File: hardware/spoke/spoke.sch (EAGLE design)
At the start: 3 parts, among them J1 ICSP, U1 ATMEGA328P_PDIP

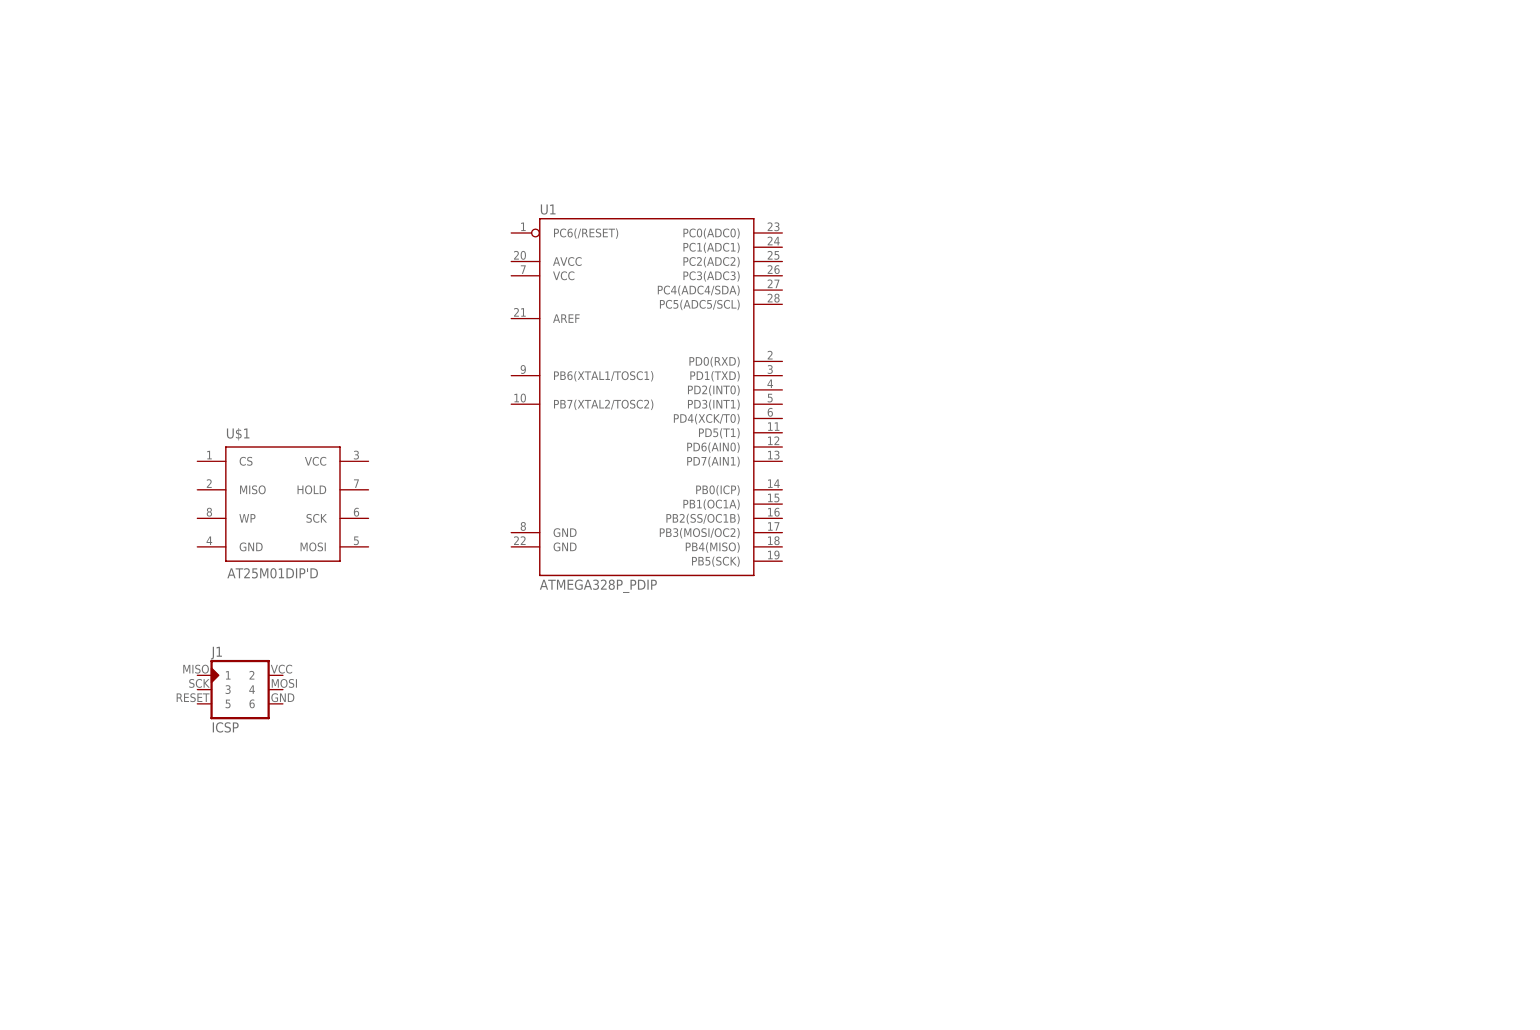
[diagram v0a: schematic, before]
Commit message: Update spoke schematic
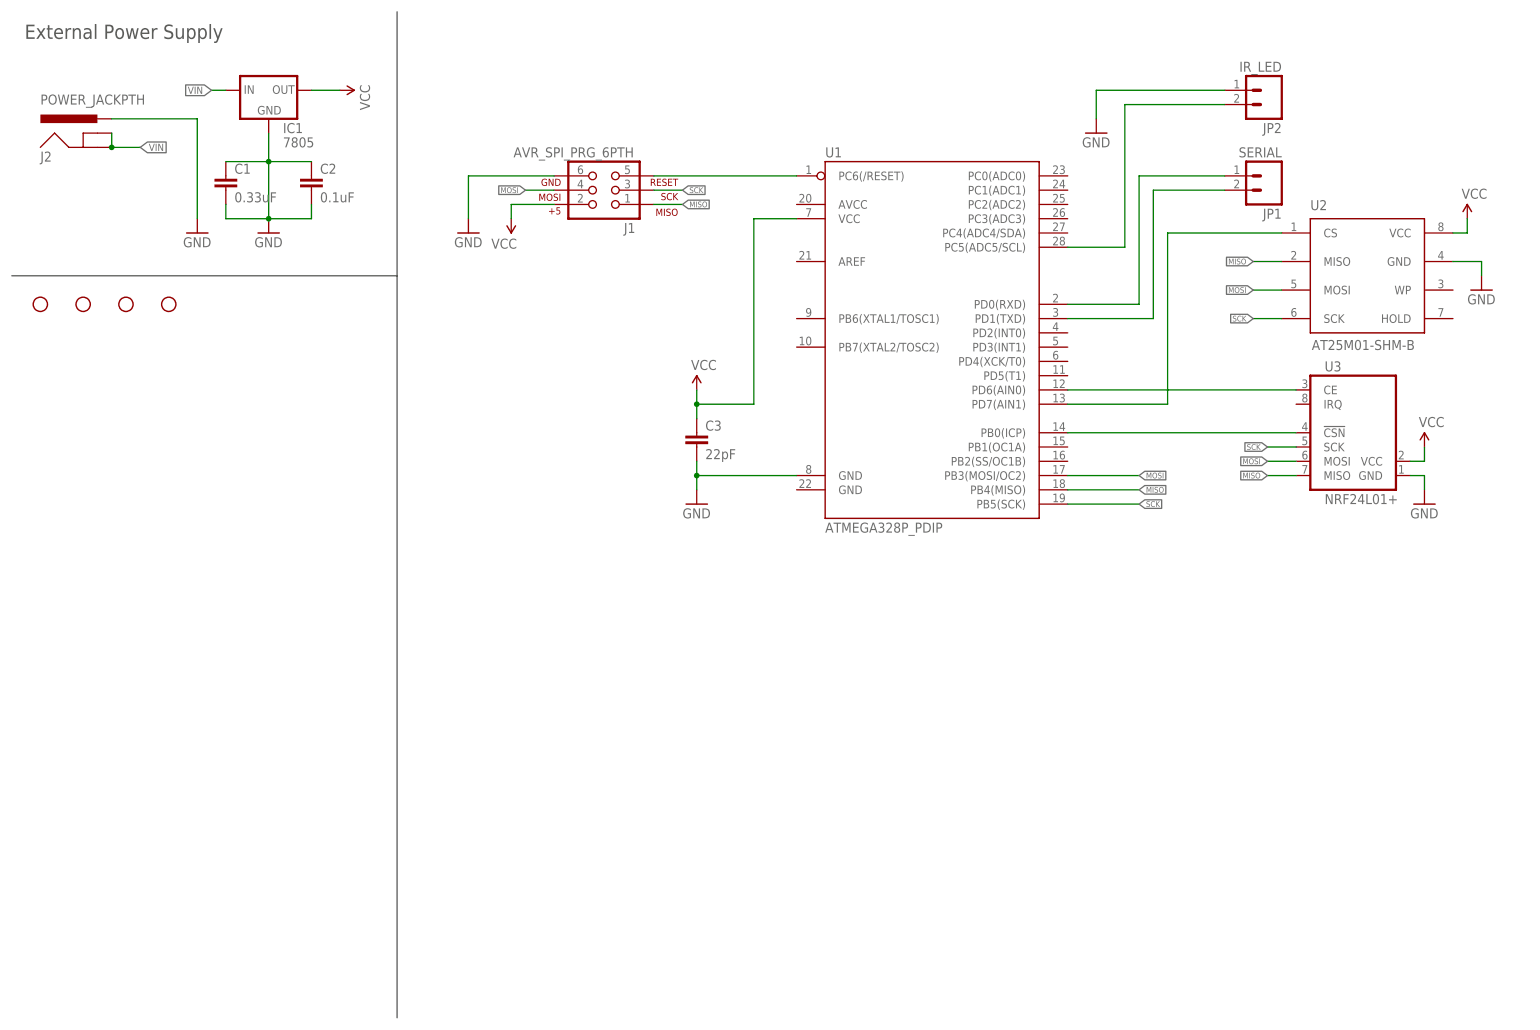
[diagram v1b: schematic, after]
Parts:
- removed U$1: AT25M01DIP'D, aurai:AT25M01DIP'D
- added C1: 0.33uF, SparkFun-Capacitors:CAPPTH
- added C2: 0.1uF, SparkFun-Capacitors:CAPPTH
- added C3: 22pF, SparkFun-Capacitors:CAPEZ
- added IC1: 7805, SparkFun-PowerIC:V_REG_78XXSINK
- added J2: POWER_JACKPTH, SparkFun-Connectors:POWER_JACKPTH
- added JP1: SERIAL, SparkFun-Connectors:M02PTH
- added JP2: IR_LED, SparkFun-Connectors:M02PTH
- added STANDOFF1, STANDOFF2, STANDOFF3, STANDOFF4: STAND-OFF, SparkFun-Electromechanical:STAND-OFF
- added U2: AT25M01-SHM-B, aurai:AT25M01-SHM-B
- added U3: NRF24L01+, aurai:NRF24L01+
- J1: value ICSP -> AVR_SPI_PRG_6PTH; device avr-isp:AVR-ISP-6PINAVR-ISP-6PIN-SMALL-SILK -> SparkFun-Connectors:AVR_SPI_PRG_6PTH
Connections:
- new net GND: C1.1, C1.2, C2.1, C2.2, C3.2, IC1.GND, J1.6, J2.PWR, JP2.1, U1.GND@1, U2.GND, U3.GND
- new net MISO: J1.1, U1.PB4(MISO), U2.MISO, U3.MISO
- new net MOSI: J1.4, U1.PB3(MOSI/OC2), U2.MOSI, U3.MOSI
- new net N$1: J1.5, U1.PC6(/RESET)
- new net N$2: JP1.1, U1.PD0(RXD)
- new net N$3: U1.PD7(AIN1), U2.CS
- new net N$4: JP1.2, U1.PD1(TXD)
- new net N$5: U1.PD6(AIN0), U3.CE
- new net N$6: JP2.2, U1.PC5(ADC5/SCL)
- new net N$7: U1.PB0(ICP), U3.!CSN
- new net SCK: J1.3, U1.PB5(SCK), U2.SCK, U3.SCK
- new net VCC: C3.1, IC1.OUT, J1.2, U1.VCC, U2.VCC, U3.VCC
- new net VIN: IC1.IN, J2.GND, J2.GNDBREAK
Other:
- note added: "External Power Supply"
- moved on the sheet: U1

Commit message: Schematic update for spoke. Added DHT-11 and LEDS
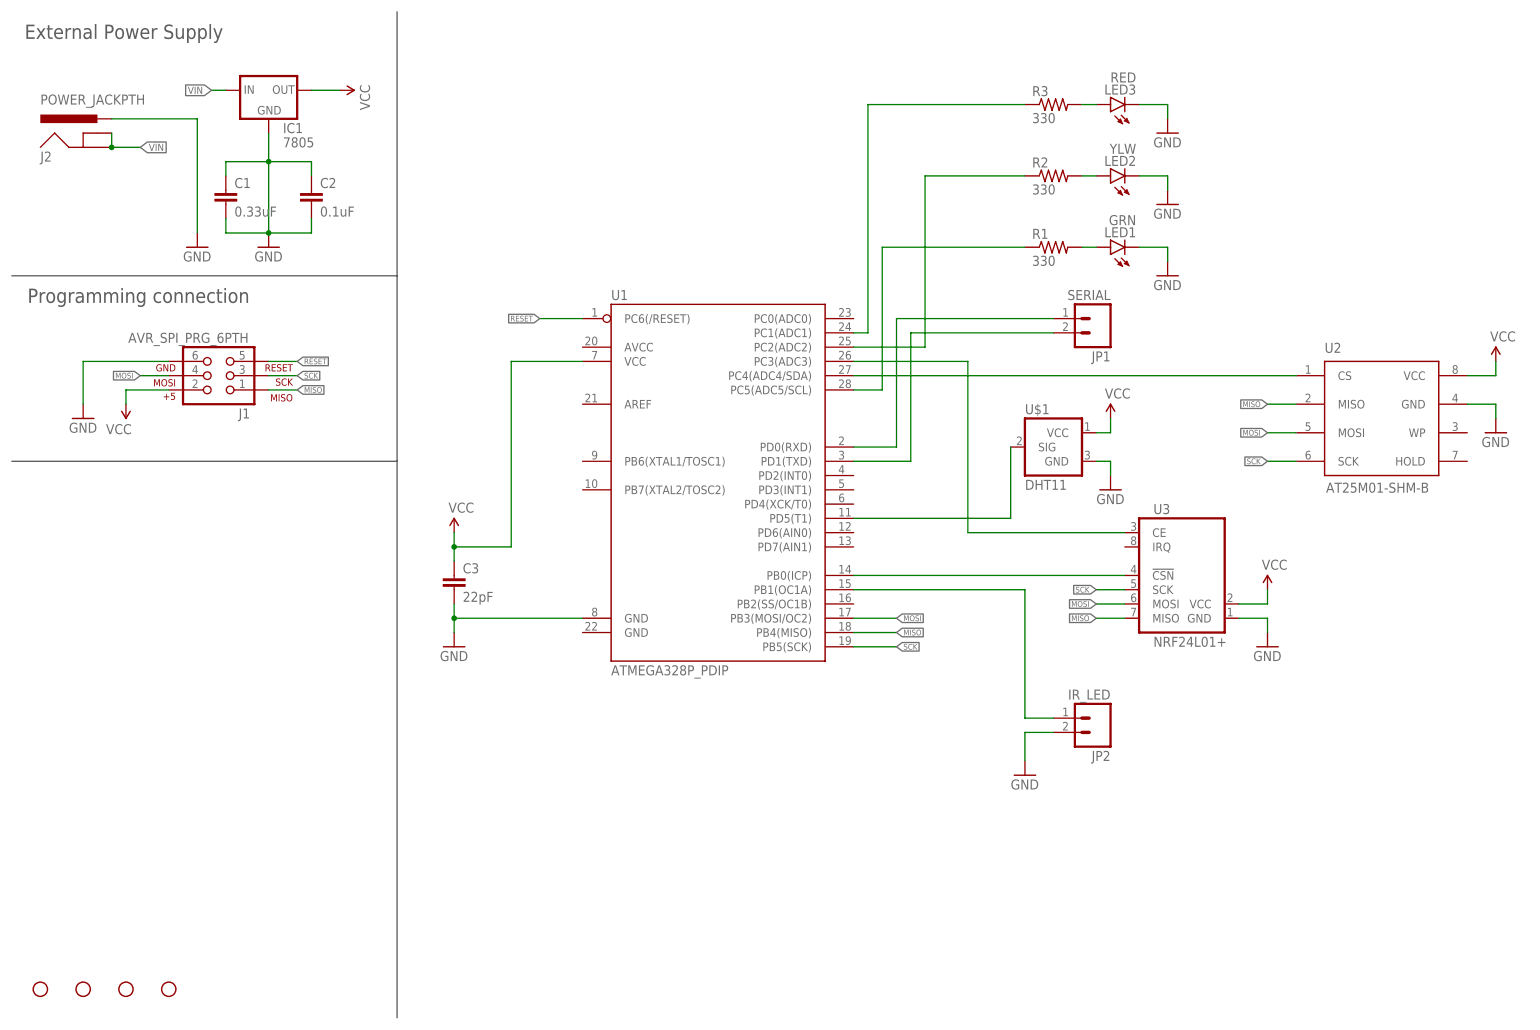
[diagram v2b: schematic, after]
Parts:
- added LED1: GRN, SparkFun-LED:LED3MM
- added LED2: YLW, SparkFun-LED:LED3MM
- added LED3: RED, SparkFun-LED:LED3MM
- added R1, R2, R3: 330, SparkFun-Passives:RESISTOREZ
- added U$1: DHT11, aurai:DHT11
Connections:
- net N$1 renamed RESET
- new net N$1: JP2.1, U1.PB1(OC1A)
- new net N$10: LED1.A, R1.2
- new net N$11: LED3.A, R3.2
- new net N$12: R1.1, U1.PC5(ADC5/SCL)
- new net N$13: R3.1, U1.PC1(ADC1)
- new net N$8: LED2.A, R2.2
- new net N$9: R2.1, U1.PC2(ADC2)
- net GND: now also JP2.2, LED1.C, LED2.C, LED3.C, U$1.GND; no longer JP2.1
- net N$3: now also U1.PC4(ADC4/SDA); no longer U1.PD7(AIN1)
- net N$5: now also U1.PC3(ADC3); no longer U1.PD6(AIN0)
- net N$6: now also U$1.SIG, U1.PD5(T1); no longer JP2.2, U1.PC5(ADC5/SCL)
- net VCC: now also U$1.VCC
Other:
- note added: "Programming connection"
- moved on the sheet: C1, C2, C3, J1, JP1, JP2, U1, U2, U3

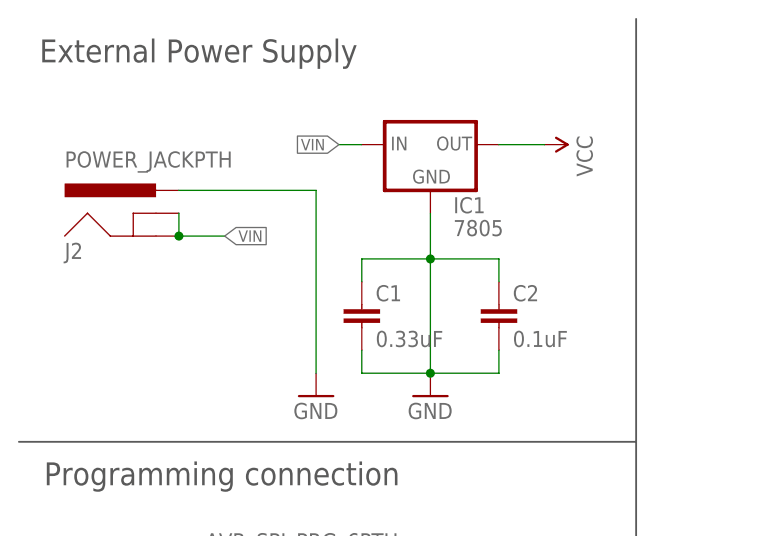
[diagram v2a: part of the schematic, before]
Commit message: Fix bad wiring in PSU
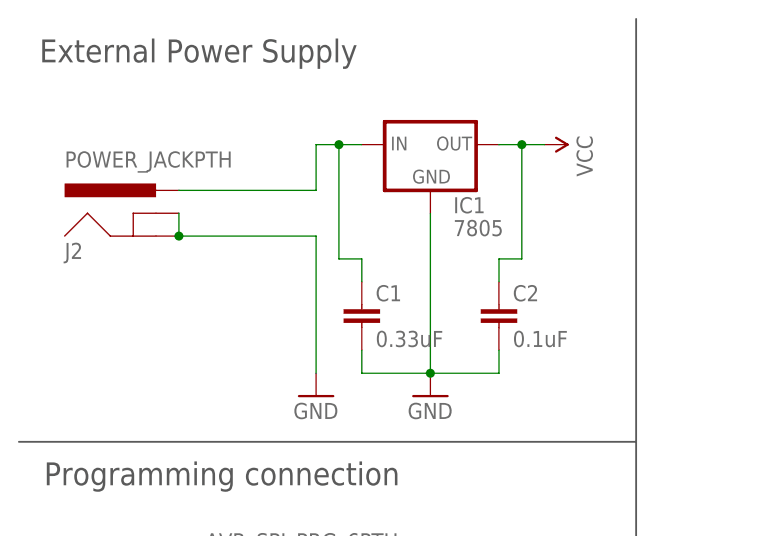
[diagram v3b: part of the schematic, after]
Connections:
- removed net VIN: IC1.IN, J2.GND, J2.GNDBREAK
- new net N$14: C1.1, IC1.IN, J2.PWR
- net GND: now also J2.GND, J2.GNDBREAK; no longer C1.1, C2.1, J2.PWR
- net VCC: now also C2.1
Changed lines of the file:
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@@
 <pinref part="IC1" gate="G$1" pin="GND"/>
 <pinref part="GND2" gate="1" pin="GND"/>
-<wire x1="45.72" y1="157.48" x2="45.72" y2="152.4" width="0.1524" layer="91"/>
-<wire x1="45.72" y1="152.4" x2="45.72" y2="139.7" width="0.1524" layer="91"/>
+<wire x1="45.72" y1="157.48" x2="45.72" y2="139.7" width="0.1524" layer="91"/>
 <wire x1="53.34" y1="139.7" x2="45.72" y2="139.7" width="0.1524" layer="91"/>
 <junction x="45.72" y="139.7"/>
@@
 <pinref part="C1" gate="G$1" pin="2"/>
 <pinref part="C2" gate="G$1" pin="2"/>
-<pinref part="C1" gate="G$1" pin="1"/>
-<wire x1="38.1" y1="149.86" x2="38.1" y2="152.4" width="0.1524" layer="91"/>
-<wire x1="38.1" y1="152.4" x2="45.72" y2="152.4" width="0.1524" layer="91"/>
-<junction x="45.72" y="152.4"/>
-<wire x1="45.72" y1="152.4" x2="53.34" y2="152.4" width="0.1524" layer="91"/>
-<pinref part="C2" gate="G$1" pin="1"/>
-<wire x1="53.34" y1="152.4" x2="53.34" y2="149.86" width="0.1524" layer="91"/>
-</segment>
-<segment>
-<pinref part="J2" gate="G$1" pin="PWR"/>
-<wire x1="17.78" y1="160.02" x2="33.02" y2="160.02" width="0.1524" layer="91"/>
-<wire x1="33.02" y1="160.02" x2="33.02" y2="139.7" width="0.1524" layer="91"/>
-<pinref part="GND3" gate="1" pin="GND"/>
 </segment>
 <segment>
@@
 <wire x1="205.74" y1="162.56" x2="205.74" y2="160.02" width="0.1524" layer="91"/>
 <pinref part="GND11" gate="1" pin="GND"/>
+</segment>
+<segment>
+<pinref part="J2" gate="G$1" pin="GNDBREAK"/>
+<pinref part="J2" gate="G$1" pin="GND"/>
+<wire x1="17.78" y1="157.48" x2="17.78" y2="154.94" width="0.1524" layer="91"/>
+<wire x1="17.78" y1="154.94" x2="33.02" y2="154.94" width="0.1524" layer="91"/>
+<junction x="17.78" y="154.94"/>
+<pinref part="GND3" gate="1" pin="GND"/>
+<wire x1="33.02" y1="154.94" x2="33.02" y2="139.7" width="0.1524" layer="91"/>
 </segment>
 </net>
@@
 </segment>
 </net>
-<net name="VIN" class="0">
-<segment>
-<pinref part="J2" gate="G$1" pin="GNDBREAK"/>
-<pinref part="J2" gate="G$1" pin="GND"/>
-<wire x1="17.78" y1="154.94" x2="17.78" y2="157.48" width="0.1524" layer="91"/>
-<wire x1="17.78" y1="154.94" x2="22.86" y2="154.94" width="0.1524" layer="91"/>
-<junction x="17.78" y="154.94"/>
-<label x="22.86" y="154.94" size="1.27" layer="95" xref="yes"/>
-</segment>
-<segment>
-<pinref part="IC1" gate="G$1" pin="IN"/>
-<wire x1="38.1" y1="165.1" x2="35.56" y2="165.1" width="0.1524" layer="91"/>
-<label x="35.56" y="165.1" size="1.27" layer="95" rot="R180" xref="yes"/>
-</segment>
-</net>
 <net name="VCC" class="0">
 <segment>
 <pinref part="IC1" gate="G$1" pin="OUT"/>
 <pinref part="SUPPLY1" gate="G$1" pin="VCC"/>
-<wire x1="53.34" y1="165.1" x2="58.42" y2="165.1" width="0.1524" layer="91"/>
+<wire x1="53.34" y1="165.1" x2="55.88" y2="165.1" width="0.1524" layer="91"/>
+<pinref part="C2" gate="G$1" pin="1"/>
+<wire x1="55.88" y1="165.1" x2="58.42" y2="165.1" width="0.1524" layer="91"/>
+<wire x1="53.34" y1="152.4" x2="53.34" y2="149.86" width="0.1524" layer="91"/>
+<wire x1="53.34" y1="152.4" x2="55.88" y2="152.4" width="0.1524" layer="91"/>
+<wire x1="55.88" y1="152.4" x2="55.88" y2="165.1" width="0.1524" layer="91"/>
+<junction x="55.88" y="165.1"/>
 </segment>
 <segment>
@@
 </segment>
 </net>
+<net name="N$14" class="0">
+<segment>
+<pinref part="IC1" gate="G$1" pin="IN"/>
+<wire x1="38.1" y1="165.1" x2="35.56" y2="165.1" width="0.1524" layer="91"/>
+<wire x1="35.56" y1="165.1" x2="33.02" y2="165.1" width="0.1524" layer="91"/>
+<wire x1="33.02" y1="165.1" x2="33.02" y2="160.02" width="0.1524" layer="91"/>
+<pinref part="J2" gate="G$1" pin="PWR"/>
+<wire x1="33.02" y1="160.02" x2="17.78" y2="160.02" width="0.1524" layer="91"/>
+<pinref part="C1" gate="G$1" pin="1"/>
+<wire x1="38.1" y1="149.86" x2="38.1" y2="152.4" width="0.1524" layer="91"/>
+<wire x1="38.1" y1="152.4" x2="35.56" y2="152.4" width="0.1524" layer="91"/>
+<wire x1="35.56" y1="152.4" x2="35.56" y2="165.1" width="0.1524" layer="91"/>
+<junction x="35.56" y="165.1"/>
+</segment>
+</net>
